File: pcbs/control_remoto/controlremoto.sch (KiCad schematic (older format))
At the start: 35 parts, among them P2 DIPSWITCH, SW1 ON/OFF, U1 PTN4050, U2 MBED, U3 ZIGBIT_DUAL_DIP

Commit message: Asociacion de componentes
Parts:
- C1: footprint (none) -> Capacitors_ThroughHole:C_Radial_D5_L6_P2.5
- C2: footprint (none) -> Discret:C1V5
- P1, P3, P4: renamed from P?; footprint (none) -> molex_2_recto
- P2: footprint (none) -> Sockets_DIP:DIP-16__300
- R1, R2, R3: footprint (none) -> Discret:R3
- SW1: footprint (none) -> PIN_ARRAY_2X1
- U1: footprint (none) -> PTN04050CAH
- U2: footprint (none) -> MBED-DOBLE
- U3: footprint (none) -> ZIGBIT_DIP_40
- U4: renamed from U?; footprint (none) -> Sockets_DIP:DIP-8__300
- gave numbers to parts that had none: 20

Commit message: Actualic? el esquematico del control remoto
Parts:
- removed C1: 100uF, Capacitors_ThroughHole:C_Radial_D5_L6_P2.5, symbol CAPAPOL
- removed C2: 100uF, Discret:C1V5, symbol CAPAPOL
- added C1, C2: 100uF, symbol C
- C3: value C -> 10u
- C4, C5: value C -> 100n
- R10, R9: value R -> 820
- R5, R7, R8: value R -> 100k
- R6: value R -> 10k
- renumbered P11 to P10, P12 to P11, P13 to P12, P2 to P13, P3 to P2, P4 to P3, P5 to P4, P6 to P5, P7 to P6, P8 to P7, P9 to P8, P10 to P9, R2 to R1, R1 to R2, U4 to U1, U1 to U2, U2 to U3, U5 to U4, U3 to U5
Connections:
- wire segments 149 -> 158

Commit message: Fin esquematico pcb control remoto
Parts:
- removed R7: 100k, symbol R
- added RV1: 100K, symbol POT
- added RV2: 100k, symbol POT
- R6: value 10k -> 1k
- R8: value 100k -> 10k
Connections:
- net labels added: VCC1, VCC2
- net labels removed: VCC
- wire segments 158 -> 161
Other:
- note added: "PARLANTE"
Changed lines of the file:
@@
 LIBS:reg104-25
 LIBS:zigbit_dual
+LIBS:lm386_mod
+LIBS:controlremoto-cache
 EELAYER 25 0
 EELAYER END
 $Descr A4 11693 8268
 encoding utf-8
-Sheet 1 1
+Sheet 1 2
 Title "Control remoto"
 Date "28 jan 2011"
@@
 TXD = RX
 $Comp
-L +5V #PWR01
+L +5V #PWR12
 U 1 1 4D407D30
 P 5200 1050
-F 0 "#PWR01" H 5200 1140 20  0001 C CNN
+F 0 "#PWR12" H 5200 1140 20  0001 C CNN
 F 1 "+5V" H 5200 1140 30  0000 C CNN
 F 2 "" H 5200 1050 60  0001 C CNN
@@
 DIPSW_1
 $Comp
-L GND #PWR02
+L GND #PWR21
 U 1 1 4D37716E
 P 10450 3300
-F 0 "#PWR02" H 10450 3300 30  0001 C CNN
+F 0 "#PWR21" H 10450 3300 30  0001 C CNN
 F 1 "GND" H 10450 3230 30  0001 C CNN
 F 2 "" H 10450 3300 60  0001 C CNN
@@
 $EndComp
 $Comp
-L +5V #PWR03
+L +5V #PWR7
 U 1 1 4D376D61
 P 3900 1200
-F 0 "#PWR03" H 3900 1290 20  0001 C CNN
+F 0 "#PWR7" H 3900 1290 20  0001 C CNN
 F 1 "+5V" H 3900 1290 30  0000 C CNN
 F 2 "" H 3900 1200 60  0001 C CNN
@@
 $EndComp
 $Comp
-L GND #PWR04
+L GND #PWR8
 U 1 1 4D3759D2
 P 3900 2050
-F 0 "#PWR04" H 3900 2050 30  0001 C CNN
+F 0 "#PWR8" H 3900 2050 30  0001 C CNN
 F 1 "GND" H 3900 1980 30  0001 C CNN
 F 2 "" H 3900 2050 60  0001 C CNN
@@
 $EndComp
 $Comp
-L GND #PWR05
+L GND #PWR4
 U 1 1 4D375976
 P 2100 1350
-F 0 "#PWR05" H 2100 1350 30  0001 C CNN
+F 0 "#PWR4" H 2100 1350 30  0001 C CNN
 F 1 "GND" H 2100 1280 30  0001 C CNN
 F 2 "" H 2100 1350 60  0001 C CNN
@@
 $EndComp
 $Comp
-L GND #PWR06
+L GND #PWR2
 U 1 1 4D3758AC
 P 1000 2050
-F 0 "#PWR06" H 1000 2050 30  0001 C CNN
+F 0 "#PWR2" H 1000 2050 30  0001 C CNN
 F 1 "GND" H 1000 1980 30  0001 C CNN
 F 2 "" H 1000 2050 60  0001 C CNN
@@
 $EndComp
 $Comp
-L +3V3 #PWR07
+L +3V3 #PWR3
 U 1 1 55036EFD
 P 1000 3350
-F 0 "#PWR07" H 1000 3200 60  0001 C CNN
+F 0 "#PWR3" H 1000 3200 60  0001 C CNN
 F 1 "+3V3" H 1000 3490 60  0000 C CNN
 F 2 "" H 1000 3350 60  0000 C CNN
@@
 $EndComp
 $Comp
-L +3V3 #PWR08
+L +3V3 #PWR5
 U 1 1 55036F39
 P 2600 3450
-F 0 "#PWR08" H 2600 3300 60  0001 C CNN
+F 0 "#PWR5" H 2600 3300 60  0001 C CNN
 F 1 "+3V3" H 2600 3590 60  0000 C CNN
 F 2 "" H 2600 3450 60  0000 C CNN
@@
 $EndComp
 $Comp
-L +3V3 #PWR09
+L +3V3 #PWR6
 U 1 1 55037478
 P 2950 2650
-F 0 "#PWR09" H 2950 2500 60  0001 C CNN
+F 0 "#PWR6" H 2950 2500 60  0001 C CNN
 F 1 "+3V3" H 2950 2790 60  0000 C CNN
 F 2 "" H 2950 2650 60  0000 C CNN
@@
 $EndComp
 $Comp
-L +3V3 #PWR010
+L +3V3 #PWR16
 U 1 1 55037912
 P 7500 950
-F 0 "#PWR010" H 7500 800 60  0001 C CNN
+F 0 "#PWR16" H 7500 800 60  0001 C CNN
 F 1 "+3V3" H 7500 1090 60  0000 C CNN
 F 2 "" H 7500 950 60  0000 C CNN
@@
 $EndComp
 $Comp
-L +3V3 #PWR011
+L +3V3 #PWR22
 U 1 1 55037C8C
 P 10750 2700
-F 0 "#PWR011" H 10750 2550 60  0001 C CNN
+F 0 "#PWR22" H 10750 2550 60  0001 C CNN
 F 1 "+3V3" H 10750 2840 60  0000 C CNN
 F 2 "" H 10750 2700 60  0000 C CNN
@@
 $EndComp
 $Comp
-L VCC #PWR012
-U 1 1 5503BEAA
-P 4950 3950
-F 0 "#PWR012" H 4950 3800 60  0001 C CNN
-F 1 "VCC" H 4950 4100 60  0000 C CNN
-F 2 "" H 4950 3950 60  0000 C CNN
-F 3 "" H 4950 3950 60  0000 C CNN
-	1    4950 3950
-	1    0    0    -1
-$EndComp
-$Comp
-L GND #PWR013
+L GND #PWR10
 U 1 1 5503C1EC
 P 4950 5100
-F 0 "#PWR013" H 4950 4850 60  0001 C CNN
+F 0 "#PWR10" H 4950 4850 60  0001 C CNN
 F 1 "GND" H 4950 4950 60  0000 C CNN
 F 2 "" H 4950 5100 60  0000 C CNN
@@
 $EndComp
 $Comp
-L R R7
-U 1 1 5503C92E
-P 5900 5750
-F 0 "R7" V 5980 5750 50  0000 C CNN
-F 1 "100k" V 5907 5751 50  0000 C CNN
-F 2 "" V 5830 5750 30  0001 C CNN
-F 3 "" H 5900 5750 30  0000 C CNN
-	1    5900 5750
-	0    -1   -1   0
-$EndComp
-$Comp
-L GND #PWR014
+L GND #PWR13
 U 1 1 5503CEBD
-P 6150 5900
-F 0 "#PWR014" H 6150 5650 60  0001 C CNN
-F 1 "GND" H 6150 5750 60  0000 C CNN
-F 2 "" H 6150 5900 60  0000 C CNN
-F 3 "" H 6150 5900 60  0000 C CNN
-	1    6150 5900
-	1    0    0    -1
-$EndComp
-$Comp
-L VCC #PWR015
-U 1 1 5503D17A
-P 5000 5900
-F 0 "#PWR015" H 5000 5750 60  0001 C CNN
-F 1 "VCC" H 5000 6050 60  0000 C CNN
-F 2 "" H 5000 5900 60  0000 C CNN
-F 3 "" H 5000 5900 60  0000 C CNN
-	1    5000 5900
-	-1   0    0    1
-$EndComp
-$Comp
-L VCC #PWR016
-U 1 1 5503D1AA
-P 6650 5850
-F 0 "#PWR016" H 6650 5700 60  0001 C CNN
-F 1 "VCC" H 6650 6000 60  0000 C CNN
-F 2 "" H 6650 5850 60  0000 C CNN
-F 3 "" H 6650 5850 60  0000 C CNN
-	1    6650 5850
-	0    1    1    0
-$EndComp
-$Comp
-L GND #PWR017
+P 6350 5900
+F 0 "#PWR13" H 6350 5650 60  0001 C CNN
+F 1 "GND" H 6350 5750 60  0000 C CNN
+F 2 "" H 6350 5900 60  0000 C CNN
+F 3 "" H 6350 5900 60  0000 C CNN
+	1    6350 5900
+	1    0    0    -1
+$EndComp
+$Comp
+L GND #PWR14
 U 1 1 5503D3DB
 P 6650 5000
-F 0 "#PWR017" H 6650 4750 60  0001 C CNN
+F 0 "#PWR14" H 6650 4750 60  0001 C CNN
 F 1 "GND" H 6650 4850 60  0000 C CNN
 F 2 "" H 6650 5000 60  0000 C CNN
@@
 P 5900 4800
 F 0 "R6" V 5980 4800 50  0000 C CNN
-F 1 "10k" V 5907 4801 50  0000 C CNN
+F 1 "1k" V 5907 4801 50  0000 C CNN
 F 2 "" V 5830 4800 30  0001 C CNN
 F 3 "" H 5900 4800 30  0000 C CNN
@@
 P 6400 4800
 F 0 "R8" V 6480 4800 50  0000 C CNN
-F 1 "100k" V 6407 4801 50  0000 C CNN
+F 1 "10k" V 6407 4801 50  0000 C CNN
 F 2 "" V 6330 4800 30  0001 C CNN
 F 3 "" H 6400 4800 30  0000 C CNN
@@
 $EndComp
 $Comp
-L GND #PWR018
+L GND #PWR17
 U 1 1 55041513
 P 7650 4600
-F 0 "#PWR018" H 7650 4350 60  0001 C CNN
+F 0 "#PWR17" H 7650 4350 60  0001 C CNN
 F 1 "GND" H 7650 4450 60  0000 C CNN
 F 2 "" H 7650 4600 60  0000 C CNN
@@
 $EndComp
 $Comp
-L GND #PWR019
+L GND #PWR20
 U 1 1 550419B8
 P 9850 4650
-F 0 "#PWR019" H 9850 4400 60  0001 C CNN
+F 0 "#PWR20" H 9850 4400 60  0001 C CNN
 F 1 "GND" H 9850 4500 60  0000 C CNN
 F 2 "" H 9850 4650 60  0000 C CNN
@@
 $EndComp
 $Comp
-L VCC #PWR020
-U 1 1 55041BEC
-P 8650 5750
-F 0 "#PWR020" H 8650 5600 60  0001 C CNN
-F 1 "VCC" H 8650 5900 60  0000 C CNN
-F 2 "" H 8650 5750 60  0000 C CNN
-F 3 "" H 8650 5750 60  0000 C CNN
-	1    8650 5750
-	-1   0    0    1
-$EndComp
-$Comp
-L GND #PWR021
+L GND #PWR18
 U 1 1 55041D07
 P 8650 4900
-F 0 "#PWR021" H 8650 4650 60  0001 C CNN
+F 0 "#PWR18" H 8650 4650 60  0001 C CNN
 F 1 "GND" H 8650 4750 60  0000 C CNN
 F 2 "" H 8650 4900 60  0000 C CNN
@@
 	3300 4500 3300 4700
 Wire Notes Line
-	600  4300 600  5800
+	600  4300 600  7650
 Wire Notes Line
 	600  5800 3900 5800
 Wire Notes Line
-	3900 5800 3900 4300
+	3900 4300 3900 7650
 Wire Notes Line
 	3900 4300 600  4300
@@
 Wire Wire Line
 	5450 4800 5750 4800
-Wire Wire Line
-	5400 5750 5750 5750
 Connection ~ 5550 5750
 Wire Wire Line
-	6150 5750 6150 5900
-Wire Wire Line
 	5000 5750 5000 5900
 Wire Wire Line
@@
 Wire Wire Line
 	6150 4800 6150 5300
-Wire Wire Line
-	6550 4800 7150 4800
-Wire Wire Line
-	7150 4800 7150 5400
 Wire Wire Line
 	7550 5400 8100 5400
@@
 Wire Wire Line
 	7650 4600 7650 4800
-Wire Wire Line
-	6050 5750 6150 5750
 Wire Wire Line
 	5100 5750 5000 5750
@@
 	850  1050 850  1300
 $Comp
-L +BATT #PWR022
+L +BATT #PWR1
 U 1 1 55264BD5
 P 800 1050
-F 0 "#PWR022" H 800 900 50  0001 C CNN
+F 0 "#PWR1" H 800 900 50  0001 C CNN
 F 1 "+BATT" H 800 1190 50  0000 C CNN
 F 2 "" H 800 1050 60  0000 C CNN
@@
 	4950 3950 4950 4300
 Wire Wire Line
-	8500 5700 8650 5700
-Wire Wire Line
-	8650 5700 8650 5750
+	8500 5700 8800 5700
 Wire Wire Line
 	6550 5800 6550 5850
 Wire Wire Line
-	6550 5850 6650 5850
+	6550 5850 6800 5850
+$Comp
+L POT RV1
+U 1 1 552858ED
+P 5900 5750
+F 0 "RV1" H 5900 5650 50  0000 C CNN
+F 1 "100K" H 5900 5750 50  0000 C CNN
+F 2 "" H 5900 5750 60  0000 C CNN
+F 3 "" H 5900 5750 60  0000 C CNN
+	1    5900 5750
+	1    0    0    -1
+$EndComp
+Wire Wire Line
+	5400 5750 5650 5750
+Wire Wire Line
+	6150 5750 6350 5750
+Wire Wire Line
+	6350 5750 6350 5900
+Wire Wire Line
+	5900 5600 5900 5500
+Connection ~ 5900 5500
+$Comp
+L POT RV2
+U 1 1 5528629C
+P 6900 4800
+F 0 "RV2" H 6900 4700 50  0000 C CNN
+F 1 "100k" H 6900 4800 50  0000 C CNN
+F 2 "" H 6900 4800 60  0000 C CNN
+F 3 "" H 6900 4800 60  0000 C CNN
+	1    6900 4800
+	1    0    0    -1
+$EndComp
+Wire Wire Line
+	6550 4800 6650 4800
+Wire Wire Line
+	6900 4650 6600 4650
+Wire Wire Line
+	6600 4650 6600 4800
+Connection ~ 6600 4800
+Wire Wire Line
+	7150 4800 7200 4800
+Wire Wire Line
+	7200 4800 7200 5400
+Connection ~ 7200 5400
+$Sheet
+S 1400 6400 950  700
+U 5528903B
+F0 "Parlante" 60
+F1 "Parlante.sch" 60
+$EndSheet
+Wire Notes Line
+	3900 7650 600  7650
+Text Notes 1700 6050 0    60   ~ 0
+PARLANTE
+Text Label 4950 3950 3    60   ~ 0
+VCC1
+Text Label 5000 5900 1    60   ~ 0
+VCC2
+Text Label 6800 5850 2    60   ~ 0
+VCC2
+Text Label 8800 5700 2    60   ~ 0
+VCC2
 $EndSCHEMATC

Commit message: agrego algunos cambios en el control y casi termino la placa principal
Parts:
- added C?: 100n, symbol C
- added L?: INDUCTOR, symbol INDUCTOR
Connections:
- net VCC1 is gone; now on net VCC2: R4.1
- net +5V: now also L?.1
- net GND: now also C?.2
- net VCC2: now also C?.1, L?.2
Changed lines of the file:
@@
 LIBS:zigbit_dual
 LIBS:lm386_mod
-LIBS:controlremoto-cache
 EELAYER 25 0
 EELAYER END
@@
 Text Label 10050 5300 2    60   ~ 0
 MIC
-Text Notes 6050 3700 0    60   ~ 0
+Text Notes 5750 3400 0    60   ~ 0
 MICROFONO
 Wire Wire Line
@@
 F0 "Parlante" 60
 F1 "Parlante.sch" 60
+F2 "VCC" I R 2350 6550 60
+F3 "GND" I R 2350 6750 60
+F4 "IN" I R 2350 6950 60
 $EndSheet
 Wire Notes Line
@@
 PARLANTE
 Text Label 4950 3950 3    60   ~ 0
-VCC1
+VCC2
 Text Label 5000 5900 1    60   ~ 0
 VCC2
@@
 Text Label 8800 5700 2    60   ~ 0
 VCC2
+$Comp
+L INDUCTOR L?
+U 1 1 55288904
+P 5900 3700
+F 0 "L?" V 5850 3700 50  0000 C CNN
+F 1 "INDUCTOR" V 6000 3700 50  0000 C CNN
+F 2 "" H 5900 3700 60  0000 C CNN
+F 3 "" H 5900 3700 60  0000 C CNN
+	1    5900 3700
+	0    -1   -1   0
+$EndComp
+$Comp
+L C C?
+U 1 1 552889EA
+P 6300 3950
+F 0 "C?" H 6350 4050 50  0000 L CNN
+F 1 "100n" H 6350 3850 50  0000 L CNN
+F 2 "" H 6338 3800 30  0001 C CNN
+F 3 "" H 6300 3950 60  0000 C CNN
+	1    6300 3950
+	1    0    0    -1
+$EndComp
+Wire Wire Line
+	6200 3700 6300 3700
+Wire Wire Line
+	6300 3700 6300 3800
+Wire Wire Line
+	6300 4100 6300 4200
+Wire Wire Line
+	5600 3700 5300 3700
+$Comp
+L GND #PWR?
+U 1 1 55288F36
+P 6300 4200
+F 0 "#PWR?" H 6300 3950 60  0001 C CNN
+F 1 "GND" H 6300 4050 60  0000 C CNN
+F 2 "" H 6300 4200 60  0000 C CNN
+F 3 "" H 6300 4200 60  0000 C CNN
+	1    6300 4200
+	1    0    0    -1
+$EndComp
+Text Label 6250 3700 0    60   ~ 0
+VCC2
+$Comp
+L +5V #PWR?
+U 1 1 552893B9
+P 5300 3700
+F 0 "#PWR?" H 5300 3790 20  0001 C CNN
+F 1 "+5V" H 5300 3790 30  0000 C CNN
+F 2 "" H 5300 3700 60  0001 C CNN
+F 3 "" H 5300 3700 60  0001 C CNN
+	1    5300 3700
+	1    0    0    -1
+$EndComp
 $EndSCHEMATC

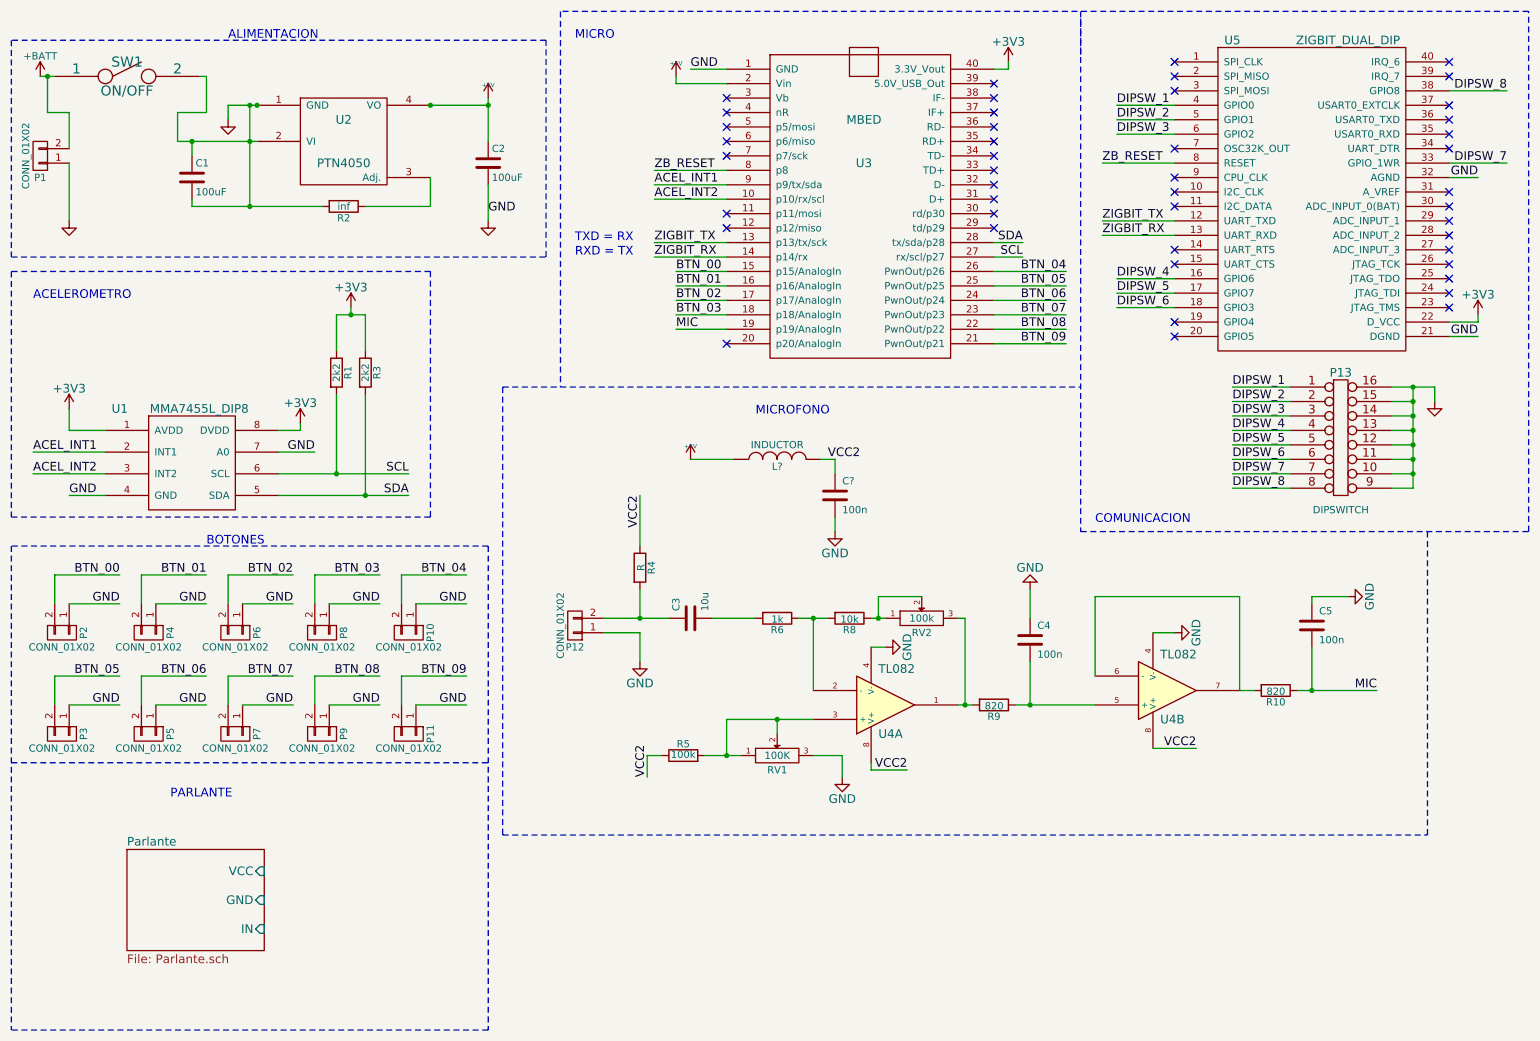
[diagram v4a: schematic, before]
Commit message: completo el esquematico del control y asigno footprints
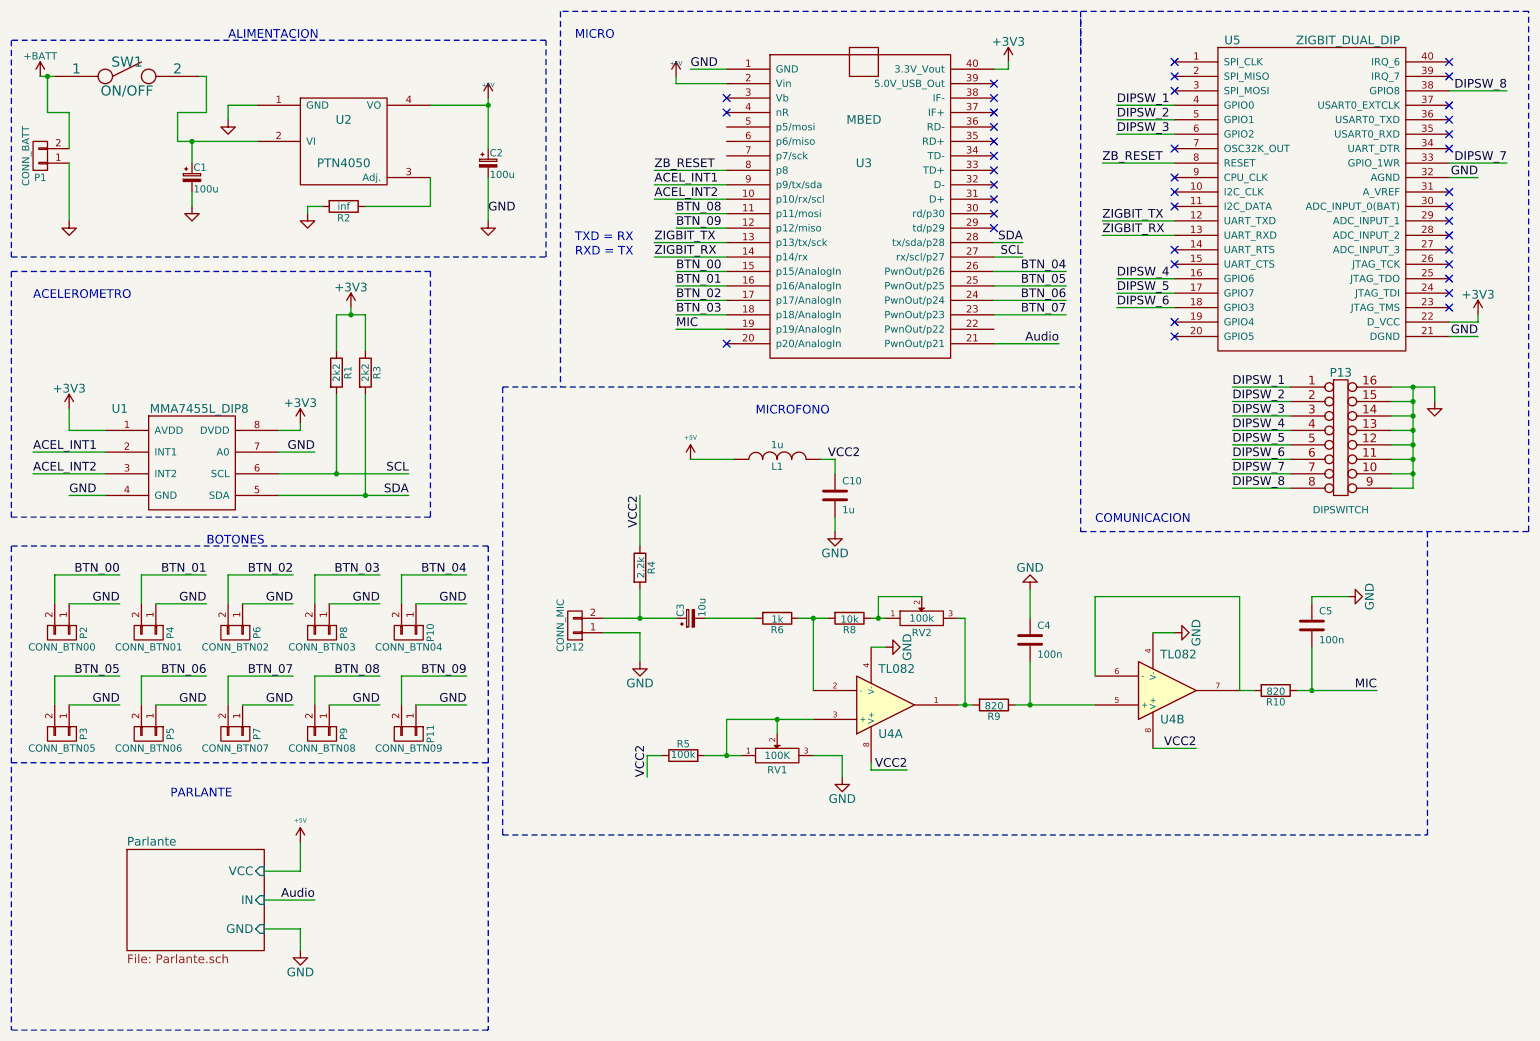
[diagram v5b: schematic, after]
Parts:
- removed C1, C2: 100uF, symbol C
- removed C3: 10u, symbol C
- added C1, C2: 100u, Capacitors_ThroughHole:C_Radial_D5_L6_P2.5, symbol CP_Small
- added C3: 10u, Capacitors_ThroughHole:C_Radial_D5_L6_P2.5, symbol CP_Small
- C10: renamed from C?; value 100n -> 1u; footprint (none) -> Capacitors_ThroughHole:C_Disc_D3_P2.5
- C4, C5: footprint (none) -> Capacitors_ThroughHole:C_Disc_D3_P2.5
- L1: renamed from L?; value INDUCTOR -> 1u; footprint (none) -> Resistors_ThroughHole:Resistor_Horizontal_RM10mm
- P1: value CONN_01X02 -> CONN_BATT; footprint molex_2_recto -> Popurri_CDR:molex_2_recto
- P10: value CONN_01X02 -> CONN_BTN04; footprint (none) -> Pin_Headers:Pin_Header_Straight_1x02
- P11: value CONN_01X02 -> CONN_BTN09; footprint (none) -> Pin_Headers:Pin_Header_Straight_1x02
- P12: value CONN_01X02 -> CONN_MIC; footprint (none) -> Connect:PINHEAD1-2
- P13: footprint Sockets_DIP:DIP-16__300 -> Sockets_DIP:DIP-16__300_ELL
- P2: value CONN_01X02 -> CONN_BTN00; footprint molex_2_recto -> Pin_Headers:Pin_Header_Straight_1x02
- P3: value CONN_01X02 -> CONN_BTN05; footprint molex_2_recto -> Pin_Headers:Pin_Header_Straight_1x02
- P4: value CONN_01X02 -> CONN_BTN01; footprint (none) -> Pin_Headers:Pin_Header_Straight_1x02
- P5: value CONN_01X02 -> CONN_BTN06; footprint (none) -> Pin_Headers:Pin_Header_Straight_1x02
- P6: value CONN_01X02 -> CONN_BTN02; footprint (none) -> Pin_Headers:Pin_Header_Straight_1x02
- P7: value CONN_01X02 -> CONN_BTN07; footprint (none) -> Pin_Headers:Pin_Header_Straight_1x02
- P8: value CONN_01X02 -> CONN_BTN03; footprint (none) -> Pin_Headers:Pin_Header_Straight_1x02
- P9: value CONN_01X02 -> CONN_BTN08; footprint (none) -> Pin_Headers:Pin_Header_Straight_1x02
- R1, R2, R3: footprint Discret:R3 -> Resistors_ThroughHole:Resistor_Horizontal_RM10mm
- R10, R5, R6, R8, R9: footprint (none) -> Resistors_ThroughHole:Resistor_Horizontal_RM10mm
- R4: value R -> 2.2k; footprint (none) -> Resistors_ThroughHole:Resistor_Horizontal_RM10mm
- RV1, RV2: footprint (none) -> Pin_Headers:Pin_Header_Straight_1x03
- SW1: footprint PIN_ARRAY_2X1 -> Pin_Headers:Pin_Header_Straight_1x02
- U1: footprint Sockets_DIP:DIP-8__300 -> Sockets_DIP:DIP-8__300_ELL
- U2: footprint PTN04050CAH -> Power_CDR:PTN04050C-EUU
- U3: footprint MBED-DOBLE -> Popurri_CDR:MBED
- U4: footprint (none) -> Sockets_DIP:DIP-8__300_ELL
- U5: footprint ZIGBIT_DIP_40 -> Popurri_CDR:ZIGBIT_DIP_40
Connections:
- net +5V: now also C2.1
- net BTN_08: now also U3.11 (p11/mosi); no longer U3.22 (PwnOut/p22)
- net BTN_09: now also U3.12 (p12/miso); no longer U3.21 (PwnOut/p21)
- net GND: now also C1.2, C2.2; no longer SW1.2, U2.2 (VI)
- net at P12.2 (P2), R4.2: now also C3.1
- net at R6.2: now also C3.2
- new net: C1.1, SW1.2, U2.2 (VI)
- new net Audio: U3.21 (PwnOut/p21)
- no-connect marks 45 -> 40
